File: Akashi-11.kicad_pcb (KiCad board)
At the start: 2 copper layers, 69.9 x 74.9 mm, 45 parts, among them CN10 PPPC192LFBN-RC, CN7 PPPC192LFBN-RC, J1 Conn_02x20_Odd_Even, SW1 SW, U1 MAX6934AQH+D, U2 MAX4719EUB+, U3 TPS613221ADBV, U4 TLV61046ADB

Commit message: Change signal name from TIM2_CH1 to TIM1_CH2
Fixed typo. The layout is not changed.
The sylkscreen of the singal is still wrong.
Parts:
- C6: value UZG0J220MCL1GB -> 22u
- C9: value UZG1H100MCL1GB -> 10u
- L1: value LQH5BPN4R7N38L -> 4.7u
- L2: value LQH5BPN100M38L -> 10u
- R2: value 61.9 -> 61.9k
- R3: value 2.15 -> 2.15k
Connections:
- net /TIM2_CH1 renamed /TIM1_CH2
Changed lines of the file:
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@@
   (net 56 "unconnected-(CN10-Pad18)")
   (net 57 "/D4")
-  (net 58 "/TIM2_CH1")
+  (net 58 "/TIM1_CH2")
   (net 59 "/D5")
   (net 60 "/TIM1_CH1")
@@
       (effects (font (size 1 1) (thickness 0.15)))
     )
-    (fp_text value "2.15" (at 0 1.43) (layer "F.Fab")
+    (fp_text value "2.15k" (at 0 1.43) (layer "F.Fab")
       (effects (font (size 1 1) (thickness 0.15)))
     )
@@
       (effects (font (size 1 1) (thickness 0.15)))
     )
-    (fp_text value "LQH5BPN100M38L" (at 0 0) (layer "F.SilkS") hide
+    (fp_text value "10u" (at 0 0) (layer "F.SilkS") hide
       (effects (font (size 1 1) (thickness 0.15)))
     )
@@
       (effects (font (size 1 1) (thickness 0.15)))
     )
-    (fp_text value "UZG0J220MCL1GB" (at 0 4.35 -90) (layer "F.Fab")
+    (fp_text value "22u" (at 0 4.35 -90) (layer "F.Fab")
       (effects (font (size 1 1) (thickness 0.15)))
     )
@@
       (net 8 "Net-(C4-Pad1)") (pintype "passive"))
     (pad "2" smd roundrect (at 0.8625 0 270) (size 1.075 0.95) (layers "F.Cu" "F.Paste" "F.Mask") (roundrect_rratio 0.25)
-      (net 58 "/TIM2_CH1") (pintype "passive"))
+      (net 58 "/TIM1_CH2") (pintype "passive"))
     (model "${KICAD6_3DMODEL_DIR}/Capacitor_SMD.3dshapes/C_0603_1608Metric.wrl"
       (offset (xyz 0 0 0))
@@
       (effects (font (size 1 1) (thickness 0.15)))
     )
-    (fp_text value "61.9" (at 0 1.43) (layer "F.Fab")
+    (fp_text value "61.9k" (at 0 1.43) (layer "F.Fab")
       (effects (font (size 1 1) (thickness 0.15)))
     )
@@
       (effects (font (size 1 1) (thickness 0.15)))
     )
-    (fp_text value "UZG1H100MCL1GB" (at 0 3.2) (layer "F.Fab")
+    (fp_text value "10u" (at 0 3.2) (layer "F.Fab")
       (effects (font (size 1 1) (thickness 0.15)))
     )
@@
       (effects (font (size 1 1) (thickness 0.15)))
     )
-    (fp_text value "LQH5BPN4R7N38L" (at 0 0) (layer "F.SilkS") hide
+    (fp_text value "4.7u" (at 0 0) (layer "F.SilkS") hide
       (effects (font (size 1 1) (thickness 0.15)))
     )
@@
     (fp_circle (center 0 0) (end 1.3 0) (layer "F.Fab") (width 0.12) (fill none))
     (pad "1" thru_hole circle (at 0 0) (size 2 2) (drill 1) (layers *.Cu *.Mask)
-      (net 58 "/TIM2_CH1") (pinfunction "1") (pintype "passive"))
+      (net 58 "/TIM1_CH2") (pinfunction "1") (pintype "passive"))
     (model "${KICAD6_3DMODEL_DIR}/TestPoint.3dshapes/TestPoint_Loop_D1.80mm_Drill1.0mm_Beaded.wrl"
       (offset (xyz 0 0 0))
@@
       (net 2 "GND") (pinfunction "Pin_20") (pintype "passive"))
     (pad "21" thru_hole oval locked (at 0 -25.4 180) (size 1.7 1.7) (drill 1) (layers *.Cu *.Mask)
-      (net 58 "/TIM2_CH1") (pinfunction "Pin_21") (pintype "passive"))
+      (net 58 "/TIM1_CH2") (pinfunction "Pin_21") (pintype "passive"))
     (pad "22" thru_hole oval locked (at -2.54 -25.4 180) (size 1.7 1.7) (drill 1) (layers *.Cu *.Mask)
       (net 123 "/KD5") (pinfunction "Pin_22") (pintype "passive"))

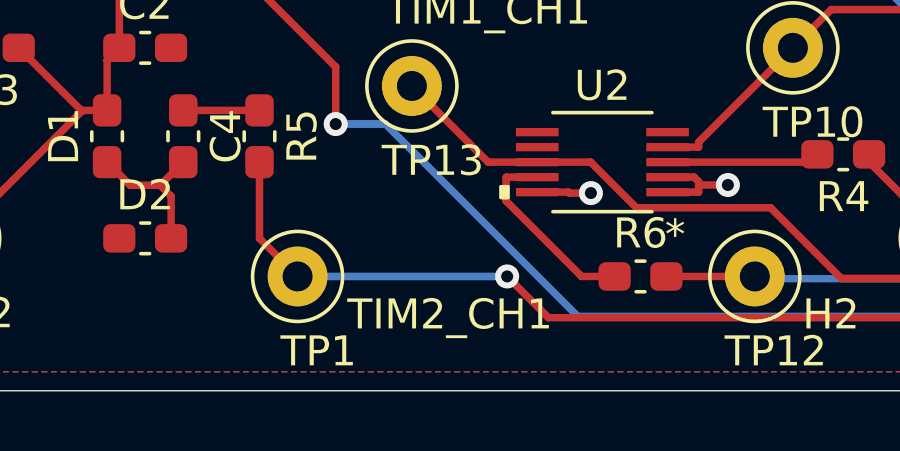
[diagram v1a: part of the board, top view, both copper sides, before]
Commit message: Modified schematics and silk.
- KEY matrix signal name is changed.
-- Including bug fix of the row order.
- R5 is changed to small resiter to fix the to small voltage.

Gerber re-generated. Schematics re-generated in PDF.
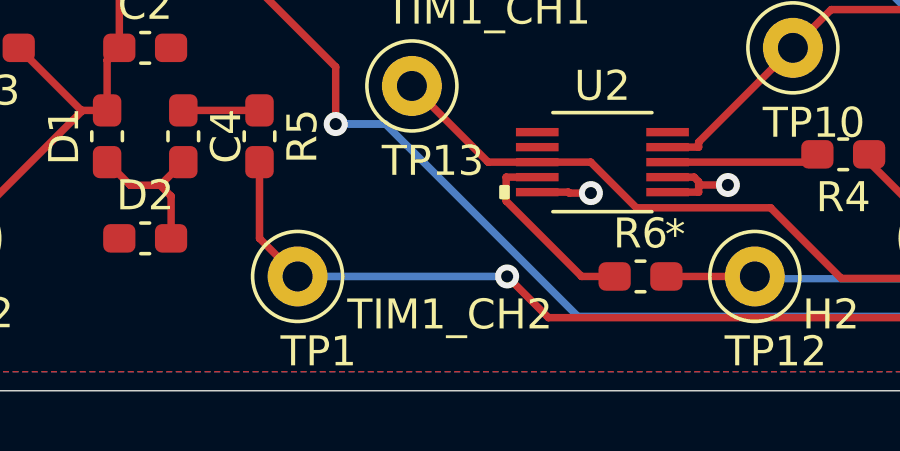
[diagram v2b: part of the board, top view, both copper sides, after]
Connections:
- net /KD0 renamed /KR8
- net /KD1 renamed /KR7
- net /KD2 renamed /KR6
- net /KD3 renamed /KR5
- net /KD4 renamed /KR4
- net /KD5 renamed /KR3
- net /KD6 renamed /KR2
- net /KD7 renamed /KR1
- net /KD8 renamed /KR0
- net /KEY1 renamed /KC0
- net /KEY2 renamed /KC1
- net /KEY3 renamed /KC2
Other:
- board text added: "Akashi-11 v1.0.1 https://github.com/suikan4github/Akashi-11 (C) Seiichi Horie 2022, 2023"
- board text added: "TIM1_CH2"
- board text removed: "Akashi-11 v1.0.0 https://github.com/suikan4github/Akashi-11 (C) Seiichi Horie 2022"
- board text removed: "TIM2_CH1"
